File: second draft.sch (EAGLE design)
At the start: 65 parts, among them IC3 74ABT125PW, Q1 NPN 40V 1A SOT-23, U1 WS2812

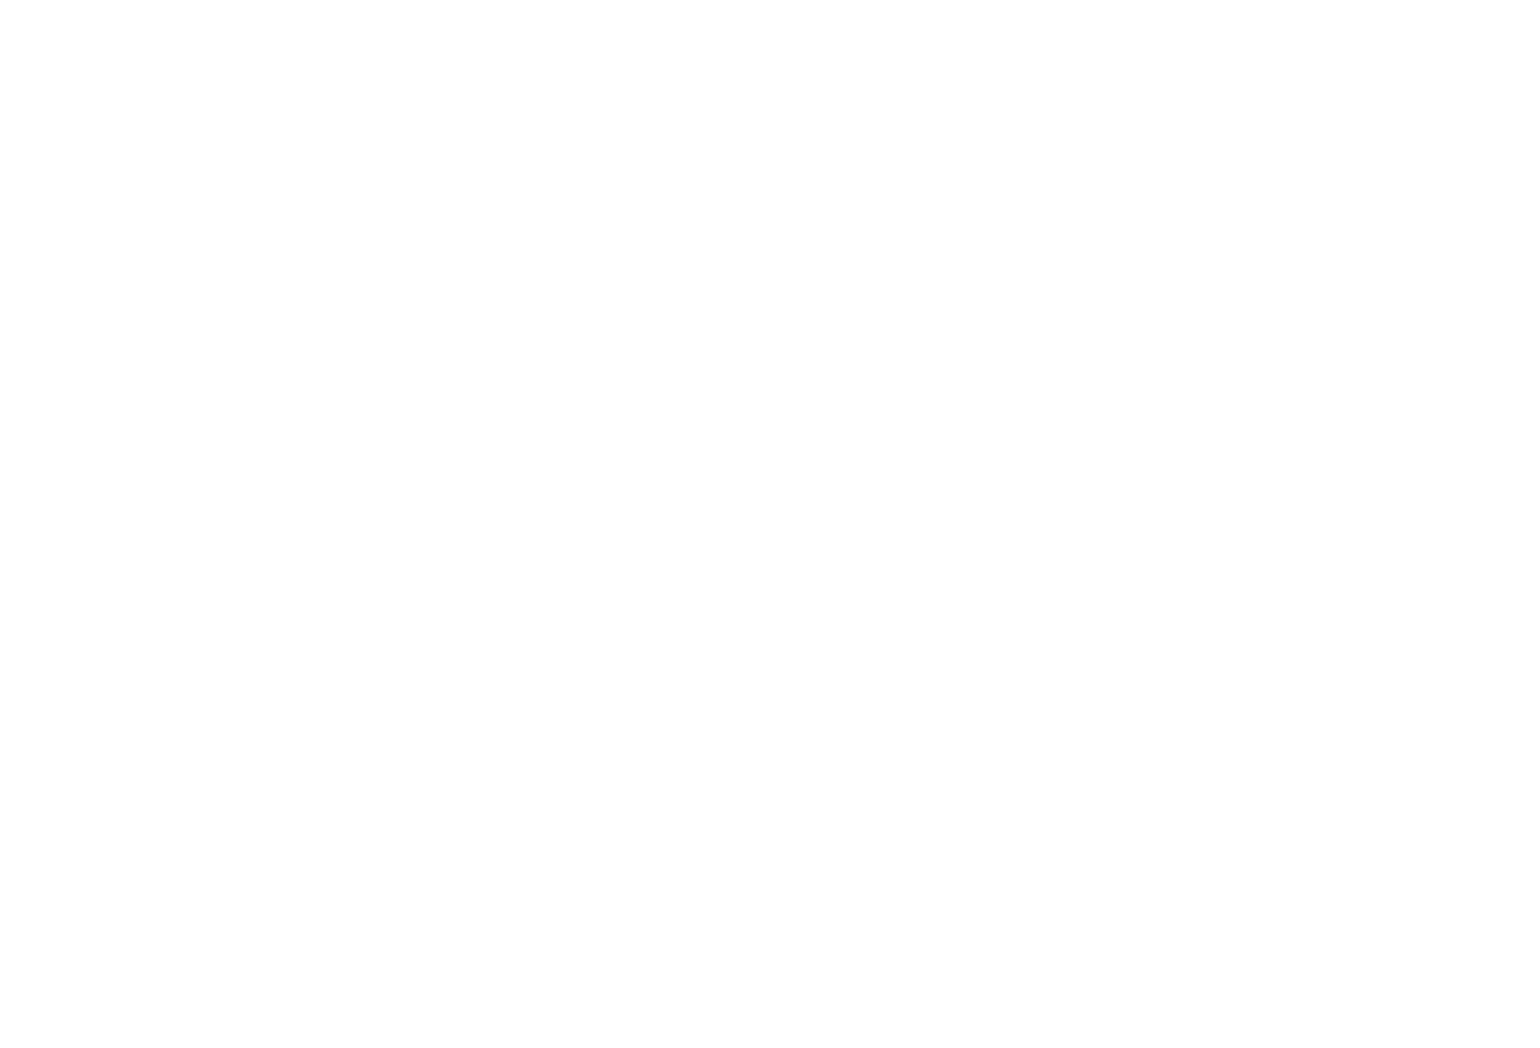
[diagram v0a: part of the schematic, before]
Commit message: added mic circuit to A6
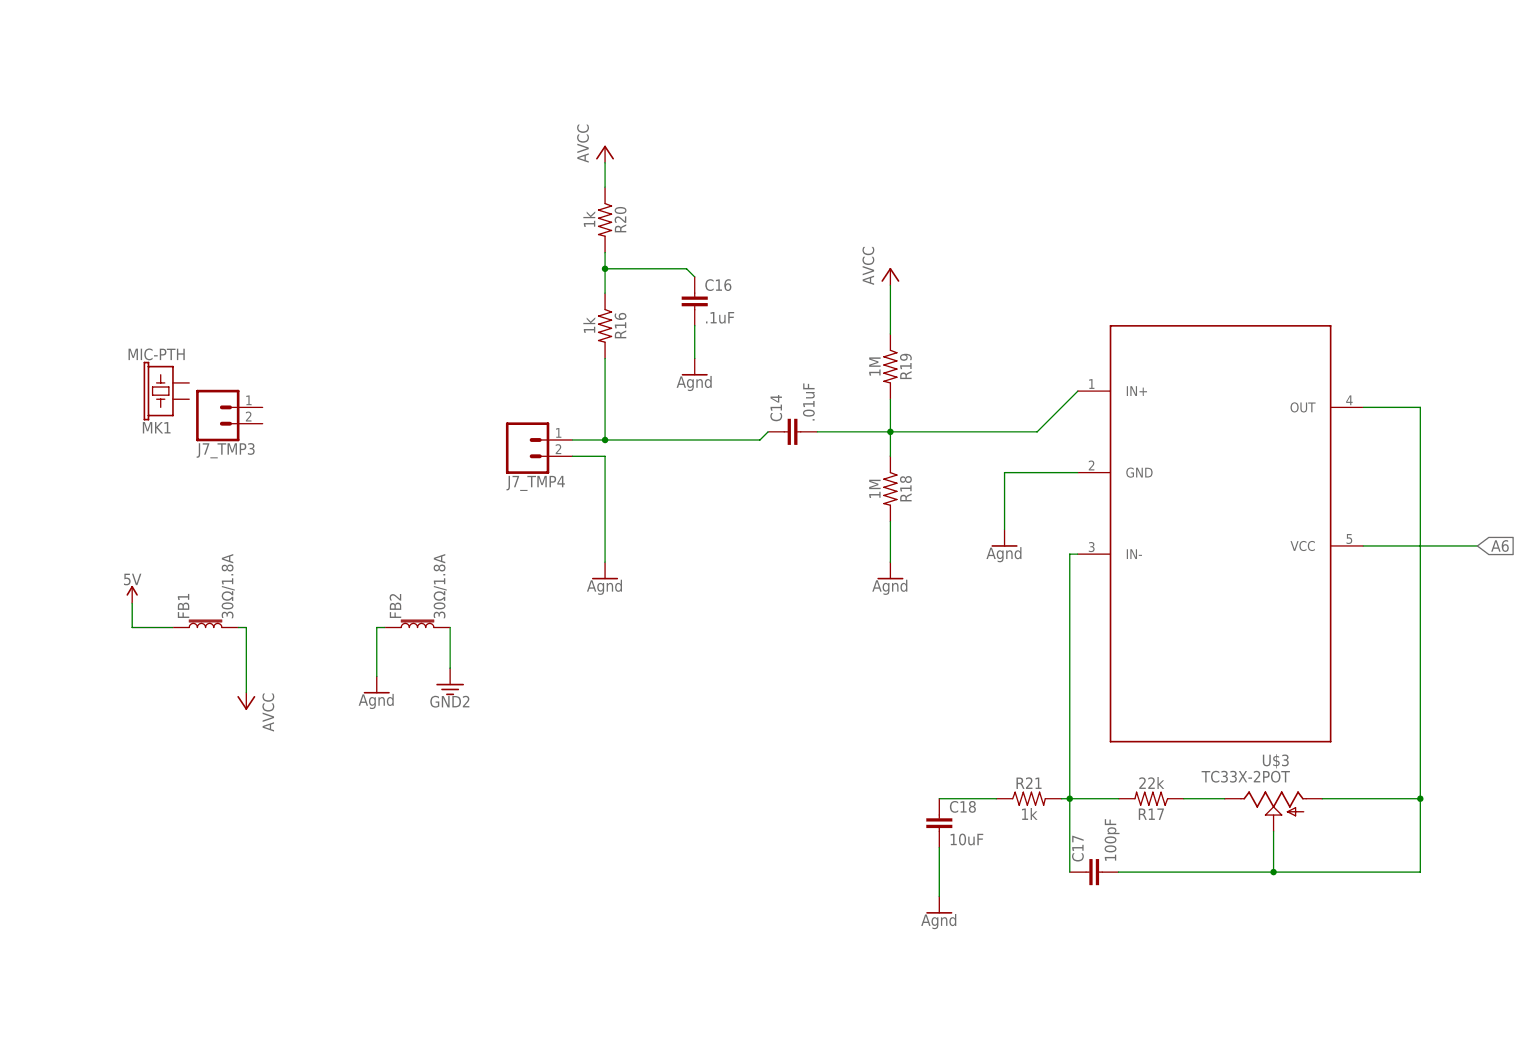
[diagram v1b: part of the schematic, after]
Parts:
- added C14: .01uF, SparkFun-Retired:.22UF-CER
- added C16: .1uF, SparkFun-Retired:.22UF-CER
- added C17: 100pF, SparkFun-Retired:.22UF-CER
- added C18: 10uF, SparkFun-Retired:.22UF-CER
- added FB1, FB2: 30Ω/1.8A, SparkFun-Coils:FERRITE_BEAD-0603
- added IC4: MAX4466KS, KevinKuwata1:MAX4466KS
- added J7_TMP3, J7_TMP4: (no value), SparkFun-Connectors:CONN_02LOCK
- added MK1: MIC-PTH, SparkFun-Sensors:MIC-PTH
- added R16, R20, R21: 1k, SparkFun-Resistors:0.05OHM-0603-1/5W-1%
- added R17: 22k, SparkFun-Resistors:0.05OHM-0603-1/5W-1%
- added R18, R19: 1M, SparkFun-Resistors:0.05OHM-0603-1/5W-1%
- added U$3: TC33X-2POT, KevinKuwata1:TC33X-2POT
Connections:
- new net N$12: R17.1, U$3.1
- new net N$17: C16.1, R16.1, R20.2
- new net N$24: C14.1, J7_TMP4.1, R16.2
- new net N$25: C14.2, IC4.IN+, R18.1, R19.2
- new net N$29: C18.1, R21.1
- new net N$30: C17.1, IC4.IN-, R17.2, R21.2
- new net N$32: C17.2, IC4.OUT, U$3.2, U$3.3
- net 3.3V: now also FB2.2
- net 5V: now also FB1.1
- net A6: now also IC4.VCC
- net GND: now also C16.2, C18.2, FB2.1, IC4.GND, J7_TMP4.2, R18.2
- net VCC: now also FB1.2, R19.1, R20.1

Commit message: added connector for mic
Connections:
- new net N$26: J7_TMP3.1, MK1.2
- new net N$27: J7_TMP3.2, MK1.1
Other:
- moved on the sheet: J7_TMP3, MK1
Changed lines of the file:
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@@
 <instance part="J8" gate="G$1" x="-160.02" y="99.06" rot="MR0"/>
 <instance part="IC4" gate="G$1" x="97.79" y="36.83" rot="R270"/>
-<instance part="MK1" gate="&gt;NAME" x="-67.31" y="57.15" rot="R90"/>
-<instance part="J7_TMP3" gate="G$1" x="-58.42" y="55.88" rot="MR180"/>
+<instance part="MK1" gate="&gt;NAME" x="-43.18" y="48.26" rot="R90"/>
+<instance part="J7_TMP3" gate="G$1" x="-22.86" y="50.8" rot="R180"/>
 <instance part="J7_TMP4" gate="G$1" x="-10.16" y="50.8" rot="MR180"/>
 <instance part="SUPPLY18" gate="G$1" x="-71.12" y="25.4"/>
@@
 </segment>
 </net>
+<net name="N$26" class="0">
+<segment>
+<pinref part="MK1" gate="&gt;NAME" pin="2"/>
+<pinref part="J7_TMP3" gate="G$1" pin="1"/>
+<wire x1="-38.1" y1="50.8" x2="-30.48" y2="50.8" width="0.1524" layer="91"/>
+</segment>
+</net>
+<net name="N$27" class="0">
+<segment>
+<pinref part="MK1" gate="&gt;NAME" pin="1"/>
+<pinref part="J7_TMP3" gate="G$1" pin="2"/>
+<wire x1="-38.1" y1="48.26" x2="-30.48" y2="48.26" width="0.1524" layer="91"/>
+</segment>
+</net>

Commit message: separated schematic in terms of items on board and off board so I could start to route
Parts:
- removed J7_TMP, J8_TMP: (no value), SparkFun-Connectors:CONN_02LOCK
- removed J8_NEO: (no value), SparkFun-Connectors:CONN_03-SCREW-5MM
- added BUZZER1: BUZZER-PTH, SparkFun-Electromechanical:BUZZER-PTH
- added D6, D7, D8, D9: LED-IRTSAL6100, SparkFun-LED:LED-IRTSAL6100
- added FB3: 30Ω/1.8A, SparkFun-Coils:FERRITE_BEAD-0603
- added IR_LED1, J3_PHOTO1, J7_BUZ1, J7_MIC1: (no value), SparkFun-Connectors:CONN_02LOCK
- added J7-TMP_B, J7-TMP_B1, J7_NEO1, J8_NEO_B, TMP-36_CONNECTOR, TMP-36_CONNECTOR1: (no value), SparkFun-Connectors:CONN_03
- added MK2: MIC-PTH, SparkFun-Sensors:MIC-PTH
- added R22: PHOTOCELLPTH-KIT, SparkFun-Sensors:PHOTOCELLPTH-KIT
- added TMP1: (no value), SparkFun-Sensors:TMP36GT9
- added U2: WS2812, SparkFun-LED:WS2812"
- J2: value (none) -> USB_MINI-B_DIGIKEY; device SparkFun-Connectors:USB_MICRO-B_SMT -> KevinKuwata1:USB_MINI-B_DIGIKEY
- J7_NEO: device SparkFun-Connectors:CONN_03-SCREW-5MM -> SparkFun-Connectors:CONN_03
- renumbered J3 to J3_PHOTO, J4 to J2PHOTO_B, J5 to J5_IR_LED_B, J6 to IR_LED, J7_TMP2 to J7_BUZ, J7_TMP3 to J7_MIC, J7_TMP4 to J7_MIC_B, J8_TMP1 to J8_BUZ_B
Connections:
- removed net TMP+: J7_TMP.1, J8_TMP.1, TMP36.VCC
- removed net TMP-: J7_TMP.2, J8_TMP.2, TMP36.GND
- new net 5V1: J7_NEO1.1, U2.DI
- new net A4: J3_PHOTO1.2, R22.P$2
- new net BUZ+1: BUZZER1.1, J7_BUZ1.1
- new net BUZ-1: BUZZER1.2, J7_BUZ1.2
- new net D1: J7_NEO1.2, U2.VDD
- new net GND1: J3_PHOTO1.1, R22.P$1
- new net GND2: J7_NEO1.3, U2.VSS
- new net N$28: D6.C, D7.A
- new net N$31: D7.C, D8.A
- new net N$33: D8.C, D9.A
- new net N$34: J7_MIC1.1, MK2.2
- new net N$35: J7_MIC1.2, MK2.1
- new net N$36: TMP-36_CONNECTOR.1, TMP36.VCC
- new net N$37: TMP-36_CONNECTOR.3, TMP36.GND
- new net N$38: TMP-36_CONNECTOR.2, TMP36.VOUT
- new net N$39: TMP-36_CONNECTOR1.1, TMP1.VCC
- new net N$40: TMP-36_CONNECTOR1.3, TMP1.GND
- new net N$41: TMP-36_CONNECTOR1.2, TMP1.VOUT
- net 3.3V: now also J7-TMP_B.3, J7-TMP_B1.3, J8_NEO_B.3; no longer J8_NEO.3
- net 5V: now also D6.A, FB3.1, IR_LED1.1, J7-TMP_B.1, J7-TMP_B1.1, J8_NEO_B.2; no longer J8_NEO.2
- net A1: now also J7-TMP_B1.2; no longer TMP36.VOUT
- net D9: now also J8_NEO_B.1; no longer J8_NEO.1
- net IR_-: now also D9.C, IR_LED1.2
- net N$16: now also FB3.2
